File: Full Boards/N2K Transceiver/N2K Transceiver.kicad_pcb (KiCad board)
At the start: 4 copper layers, 80 x 60 mm, 77 parts, among them J1 Optional Bond, J2 PSU TP, J3 JTAG, SW1 SW_MEC_5G, SW2 SW_MEC_5G, SW3 SW_MEC_5G

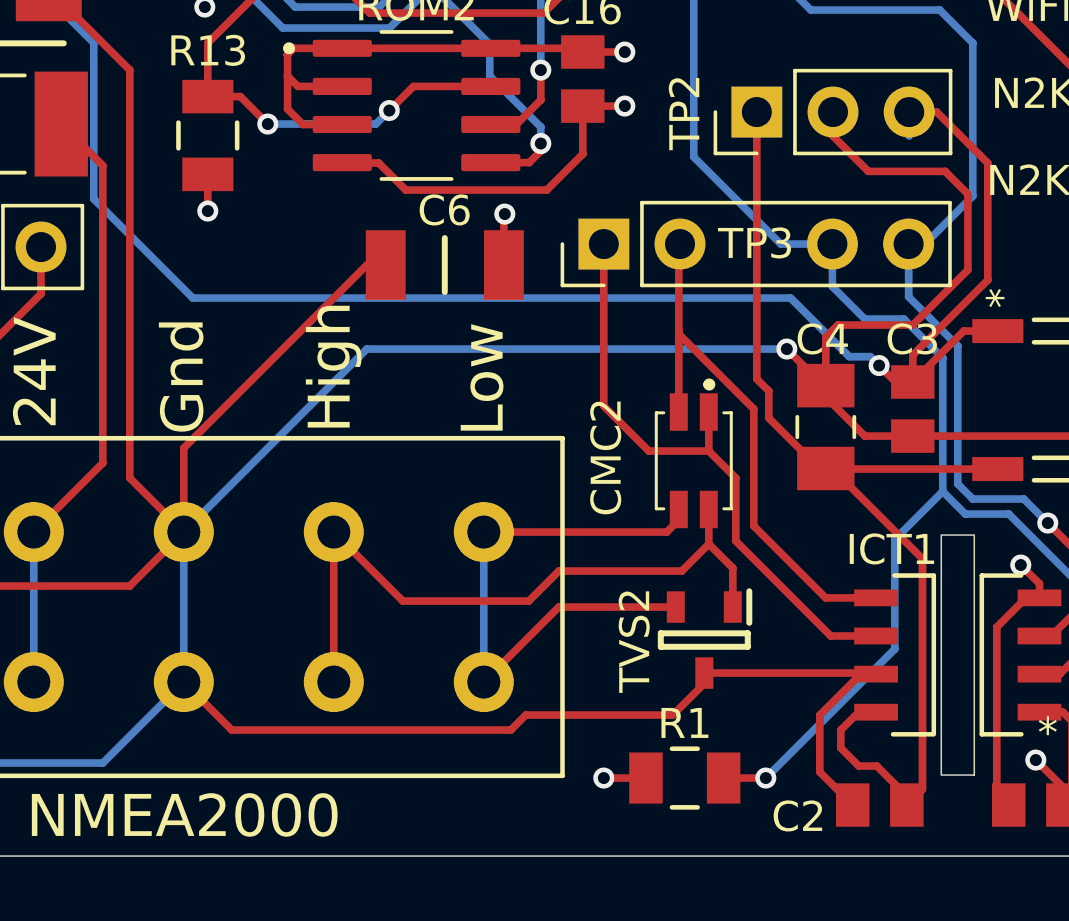
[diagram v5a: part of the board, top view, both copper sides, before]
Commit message: Reworked the CAN TVS/CMC to help balance lead length.
Signed-off-by: digimer <digital.mermaid@gmail.com>
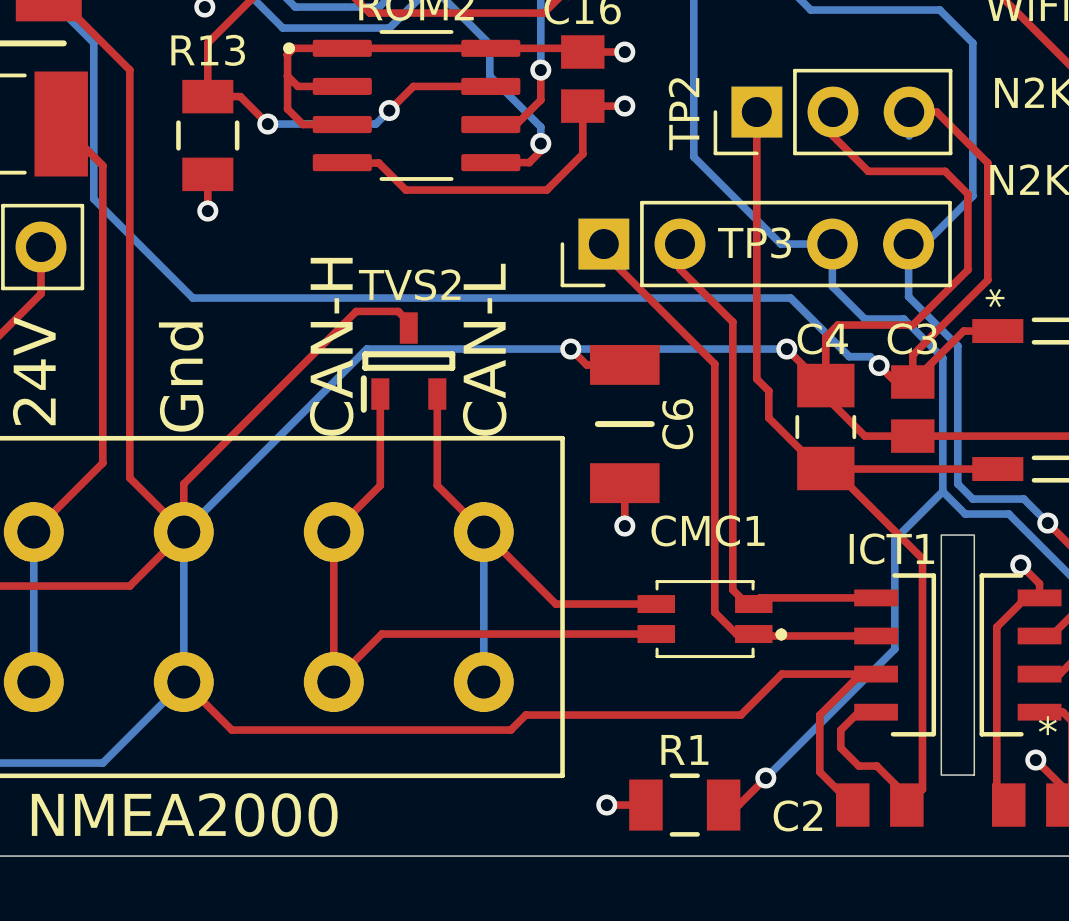
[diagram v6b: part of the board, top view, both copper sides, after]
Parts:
- moved TVS2 13.5 mm to (107.1, 86.8), turned to 90 degrees
- moved C6 8.01 mm to (114.3, 88.9), turned to 90 degrees
- moved CMC1 5.53 mm to (117.2, 95.4), turned to 180 degrees
- moved R1 0.90 mm to (116.3, 101.6)
- renumbered CMC2 to CMC1
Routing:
- net Net-(CMC1-O2): track 19.5 -> 17.0 mm
- net GND_SHIP: track 188.1 -> 189.7 mm, vias 23 -> 24
- net /CAN_LOW: track 18.5 -> 17.4 mm
- net Net-(CMC1-O1): track 22.8 -> 21.7 mm
- net /CAN_HIGH: track 20.5 -> 19.5 mm
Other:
- board text added: "CAN-H"
- board text added: "CAN-L"
- board text removed: "High"
- board text removed: "Low"

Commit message: Further tuning of the CAN bus traces.
Signed-off-by: digimer <digital.mermaid@gmail.com>
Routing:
- net Net-(CMC1-O2): track 17.0 -> 22.4 mm
- net Net-(CMC1-O1): track 21.7 -> 23.0 mm
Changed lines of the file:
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@@
-	)
-	(segment
-		(start 89.599999 92.5)
-		(end 89.599999 97.5)
-		(width 0.254)
-		(layer "F.Cu")
-		(net "Net-(J1-Pin_1)")
 	)
 	(segment
@@
 		(width 0.254)
 		(layer "F.Cu")
+		(net "Net-(J1-Pin_1)")
+	)
+	(segment
+		(start 89.599999 92.5)
+		(end 89.599999 97.5)
+		(width 0.254)
+		(layer "B.Cu")
 		(net "Net-(J1-Pin_1)")
 	)
@@
 	)
 	(segment
-		(start 104.6 97.5)
-		(end 104.6 92.5)
+		(start 106.5 94.6)
+		(end 106.5 93.6)
+		(width 0.254)
+		(layer "F.Cu")
+		(net "Net-(CMC1-O1)")
+	)
+	(segment
+		(start 107.8 95.9)
+		(end 106.5 94.6)
+		(width 0.254)
+		(layer "F.Cu")
+		(net "Net-(CMC1-O1)")
+	)
+	(segment
+		(start 106.5 93.6)
+		(end 105.4 92.5)
 		(width 0.254)
 		(layer "F.Cu")
@@
 	(segment
 		(start 115.35 95.9)
-		(end 106.2 95.9)
+		(end 107.8 95.9)
+		(width 0.254)
+		(layer "F.Cu")
+		(net "Net-(CMC1-O1)")
+	)
+	(segment
+		(start 105.4 92.5)
+		(end 104.6 92.5)
 		(width 0.254)
 		(layer "F.Cu")
@@
 	)
 	(segment
-		(start 106.2 95.9)
+		(start 104.6 92.5)
 		(end 104.6 97.5)
 		(width 0.254)
-		(layer "F.Cu")
+		(layer "B.Cu")
 		(net "Net-(CMC1-O1)")
 	)
 	(segment
-		(start 112 94.9)
-		(end 115.35 94.9)
+		(start 109.6 92.5)
+		(end 108.05 90.95)
 		(width 0.254)
 		(layer "F.Cu")
@@
 	)
 	(segment
-		(start 109.6 92.5)
-		(end 108.05 90.95)
+		(start 108.2 92.5)
+		(end 109.6 92.5)
+		(width 0.254)
+		(layer "F.Cu")
+		(net "Net-(CMC1-O2)")
+	)
+	(segment
+		(start 107.2 94.5)
+		(end 107.2 93.5)
+		(width 0.254)
+		(layer "F.Cu")
+		(net "Net-(CMC1-O2)")
+	)
+	(segment
+		(start 115.35 94.9)
+		(end 107.6 94.9)
 		(width 0.254)
 		(layer "F.Cu")
@@
 	)
 	(segment
-		(start 109.6 92.5)
-		(end 112 94.9)
+		(start 107.6 94.9)
+		(end 107.2 94.5)
 		(width 0.254)
 		(layer "F.Cu")
+		(net "Net-(CMC1-O2)")
+	)
+	(segment
+		(start 107.2 93.5)
+		(end 108.2 92.5)
+		(width 0.254)
+		(layer "F.Cu")

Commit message: Refactoring to remove isolation. the real world benefits of isolation are weaker than the benefits of better energy efficiency. This also allows claiming LEN 1 on NMEA2000 instead of LEN 2.
Signed-off-by: digimer <digital.mermaid@gmail.com>
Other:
- board text added: "NMEA2000 LEN: 2"
- board text removed: "NMEA2000"
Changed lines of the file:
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@@
 		(tags "1862440 ")
 		(property "Reference" "TB1"
-			(at -21.2 4.1 0)
+			(at -23.5 -2.3 90)
 			(unlocked yes)
 			(layer "F.SilkS")
@@
 		)
 	)
-	(gr_text "NMEA2000"
-		(at 99.6 102.8 0)
+	(gr_text "NMEA2000  LEN: 2"
+		(at 99.4 102.7 0)
 		(layer "F.SilkS")
 		(effects
@@
 	)
 	(segment
-		(start 120.782 90.382)
-		(end 119.1 88.7)
-		(width 0.254)
-		(layer "F.Cu")
-		(net "+5V_SHIP")
-	)
-	(segment
 		(start 122.1 100.3)
 		(end 121.5 99.7)
@@
 	)
 	(segment
-		(start 119.1 88.7)
-		(end 119.1 87.8)
-		(width 0.254)
-		(layer "F.Cu")
-		(net "+5V_SHIP")
-	)
-	(segment
 		(start 124.202421 93.370442)
 		(end 124.223 93.393867)
@@
 	)
 	(segment
-		(start 118.7 87.4)
-		(end 118.7 78.5)
-		(width 0.254)
-		(layer "F.Cu")
-		(net "+5V_SHIP")
-	)
-	(segment
 		(start 123.7017 101.3017)
 		(end 122.7 100.3)
@@
 	)
 	(segment
-		(start 121.5 99.7)
-		(end 121.5 99.1)
+		(start 120.782 90.382)
+		(end 118.7 88.3)
 		(width 0.254)
 		(layer "F.Cu")
@@
 	)
 	(segment
-		(start 119.1 87.8)
-		(end 118.7 87.4)
+		(start 121.5 99.7)
+		(end 121.5 99.1)
 		(width 0.254)
 		(layer "F.Cu")
@@
 		(width 0.254)
 		(layer "F.Cu")
+		(net "+5V_SHIP")
+	)
+	(segment
+		(start 118.7 88.3)
+		(end 118.7 78.5)
+		(width 0.254)
+		(layer "F.Cu")
